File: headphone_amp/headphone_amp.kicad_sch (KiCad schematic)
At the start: 31 parts, among them J1 POWER, J2 INPUT, J3 PHONES, U1 LDL1117S50R, U2 LM4808

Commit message: Use kosmo-lib. Export PDF
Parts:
- removed U2: LM4808, Package_SO:SOIC-8_3.9x4.9mm_P1.27mm, symbol headphone_amp:LM4808
- added U2: LM4808, Package_SO:SOIC-8_3.9x4.9mm_P1.27mm, symbol kosmo-lib:LM4808
- RV1: footprint headphone_amp:Pot_Bourns_PTD902 -> kosmo-lib:Pot_Bourns_PTD902
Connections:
- net +5V: now also U2.8 (VDD)
- net AMP_BIAS: now also U2.3 (IN_A+), U2.5 (IN_B+)
- net AMP_IN_L: now also U2.2 (IN_A-)
- net AMP_IN_R: now also U2.6 (IN_B-)
- net AMP_OUT_L: now also U2.1 (OUT_A)
- net AMP_OUT_R: now also U2.7 (OUT_B)
- net GND: now also U2.4 (GND)
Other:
- company: (none) -> Max Proskauer
- title: (none) -> LM4808 Headphone Amp Module
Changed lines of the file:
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@@
 (kicad_sch (version 20211123) (generator eeschema)
   (paper "USLetter")
+  (title_block
+    (title "LM4808 Headphone Amp Module")
+    (date "2022-05-30")
+    (rev "0.1")
+    (company "Max Proskauer")
+  )
   (junction (at 91.44 158.75) (diameter 0) (color 0 0 0 0)
   )
@@
     (pin "1")
   )
-  (symbol (lib_id "Device:R") (at 86.36 83.82 0) (unit 1)
-    (in_bom yes) (on_board yes) (fields_autoplaced)
-    (property "Reference" "R2" (id 0) (at 88.9 82.5499 0)
-      (effects (font (size 1.27 1.27)) (justify left))
-    )
-    (property "Value" "100k" (id 1) (at 88.9 85.0899 0)
-      (effects (font (size 1.27 1.27)) (justify left))
-    )
-    (property "Footprint" "Resistor_THT:R_Axial_DIN0207_L6.3mm_D2.5mm_P10.16mm_Horizontal" (id 2) (at 84.582 83.82 90)
-      (effects (font (size 1.27 1.27)) hide)
-    )
-    (property "Datasheet" "~" (id 3) (at 86.36 83.82 0)
-      (effects (font (size 1.27 1.27)) hide)
-    )
-    (pin "1")
-    (pin "2")
-  )
-  (symbol (lib_id "Device:R_Potentiometer_Dual") (at 60.96 77.47 270) (mirror x) (unit 1)
-    (in_bom yes) (on_board yes)
-    (property "Reference" "RV1" (id 0) (at 54.61 69.85 90)
-      (effects (font (size 1.27 1.27)) (justify right))
-    )
-    (property "Value" "10k" (id 1) (at 54.61 72.39 90)
-      (effects (font (size 1.27 1.27)) (justify right))
-    )
-    (property "Footprint" "headphone_amp:Pot_Bourns_PTD902" (id 2) (at 59.055 71.12 0)
-      (effects (font (size 1.27 1.27)) hide)
-    )
-    (property "Datasheet" "~" (id 3) (at 59.055 71.12 0)
-      (effects (font (size 1.27 1.27)) hide)
-    )
-    (pin "1")
-    (pin "2")
-    (pin "3")
-    (pin "4")
-    (pin "5")
-    (pin "6")
-  )
-  (symbol (lib_id "Device:D") (at 201.93 115.57 270) (unit 1)
-    (in_bom yes) (on_board yes) (fields_autoplaced)
-    (property "Reference" "D5" (id 0) (at 204.47 114.2999 90)
-      (effects (font (size 1.27 1.27)) (justify left))
-    )
-    (property "Value" "1N4148" (id 1) (at 204.47 116.8399 90)
-      (effects (font (size 1.27 1.27)) (justify left))
-    )
-    (property "Footprint" "Diode_THT:D_DO-34_SOD68_P7.62mm_Horizontal" (id 2) (at 201.93 115.57 0)
-      (effects (font (size 1.27 1.27)) hide)
-    )
-    (property "Datasheet" "~" (id 3) (at 201.93 115.57 0)
-      (effects (font (size 1.27 1.27)) hide)
-    )
-    (pin "1")
-    (pin "2")
-  )
-  (symbol (lib_id "power:-12V") (at 201.93 58.42 180) (unit 1)
-    (in_bom yes) (on_board yes)
-    (property "Reference" "#PWR021" (id 0) (at 201.93 60.96 0)
-      (effects (font (size 1.27 1.27)) hide)
-    )
-    (property "Value" "-12V" (id 1) (at 201.93 62.23 0))
-    (property "Footprint" "" (id 2) (at 201.93 58.42 0)
-      (effects (font (size 1.27 1.27)) hide)
-    )
-    (property "Datasheet" "" (id 3) (at 201.93 58.42 0)
-      (effects (font (size 1.27 1.27)) hide)
-    )
-    (pin "1")
-  )
-  (symbol (lib_id "headphone_amp:LM4808") (at 140.97 77.47 0) (unit 1)
+  (symbol (lib_id "kosmo-lib:LM4808") (at 140.97 77.47 0) (unit 1)
     (in_bom yes) (on_board yes)
     (property "Reference" "U2" (id 0) (at 132.08 57.15 0)
@@
     (pin "7")
     (pin "8")
+  )
+  (symbol (lib_id "Device:R") (at 86.36 83.82 0) (unit 1)
+    (in_bom yes) (on_board yes) (fields_autoplaced)
+    (property "Reference" "R2" (id 0) (at 88.9 82.5499 0)
+      (effects (font (size 1.27 1.27)) (justify left))
+    )
+    (property "Value" "100k" (id 1) (at 88.9 85.0899 0)
+      (effects (font (size 1.27 1.27)) (justify left))
+    )
+    (property "Footprint" "Resistor_THT:R_Axial_DIN0207_L6.3mm_D2.5mm_P10.16mm_Horizontal" (id 2) (at 84.582 83.82 90)
+      (effects (font (size 1.27 1.27)) hide)
+    )
+    (property "Datasheet" "~" (id 3) (at 86.36 83.82 0)
+      (effects (font (size 1.27 1.27)) hide)
+    )
+    (pin "1")
+    (pin "2")
+  )
+  (symbol (lib_id "Device:R_Potentiometer_Dual") (at 60.96 77.47 270) (mirror x) (unit 1)
+    (in_bom yes) (on_board yes)
+    (property "Reference" "RV1" (id 0) (at 54.61 69.85 90)
+      (effects (font (size 1.27 1.27)) (justify right))
+    )
+    (property "Value" "10k" (id 1) (at 54.61 72.39 90)
+      (effects (font (size 1.27 1.27)) (justify right))
+    )
+    (property "Footprint" "kosmo-lib:Pot_Bourns_PTD902" (id 2) (at 59.055 71.12 0)
+      (effects (font (size 1.27 1.27)) hide)
+    )
+    (property "Datasheet" "~" (id 3) (at 59.055 71.12 0)
+      (effects (font (size 1.27 1.27)) hide)
+    )
+    (pin "1")
+    (pin "2")
+    (pin "3")
+    (pin "4")
+    (pin "5")
+    (pin "6")
+  )
+  (symbol (lib_id "Device:D") (at 201.93 115.57 270) (unit 1)
+    (in_bom yes) (on_board yes) (fields_autoplaced)
+    (property "Reference" "D5" (id 0) (at 204.47 114.2999 90)
+      (effects (font (size 1.27 1.27)) (justify left))
+    )
+    (property "Value" "1N4148" (id 1) (at 204.47 116.8399 90)
+      (effects (font (size 1.27 1.27)) (justify left))
+    )
+    (property "Footprint" "Diode_THT:D_DO-34_SOD68_P7.62mm_Horizontal" (id 2) (at 201.93 115.57 0)
+      (effects (font (size 1.27 1.27)) hide)
+    )
+    (property "Datasheet" "~" (id 3) (at 201.93 115.57 0)
+      (effects (font (size 1.27 1.27)) hide)
+    )
+    (pin "1")
+    (pin "2")
+  )
+  (symbol (lib_id "power:-12V") (at 201.93 58.42 180) (unit 1)
+    (in_bom yes) (on_board yes)
+    (property "Reference" "#PWR021" (id 0) (at 201.93 60.96 0)
+      (effects (font (size 1.27 1.27)) hide)
+    )
+    (property "Value" "-12V" (id 1) (at 201.93 62.23 0))
+    (property "Footprint" "" (id 2) (at 201.93 58.42 0)
+      (effects (font (size 1.27 1.27)) hide)
+    )
+    (property "Datasheet" "" (id 3) (at 201.93 58.42 0)
+      (effects (font (size 1.27 1.27)) hide)
+    )
+    (pin "1")
   )
   (symbol (lib_id "power:+12V") (at 91.44 156.21 0) (unit 1)
@@
     )
     (path "/1eaa0cb5-51d1-4401-b7ff-689d85613c1f"
-      (reference "RV1") (unit 1) (value "10k") (footprint "headphone_amp:Pot_Bourns_PTD902")
+      (reference "RV1") (unit 1) (value "10k") (footprint "kosmo-lib:Pot_Bourns_PTD902")
     )
     (path "/05cac65d-cafa-4294-bc5f-223d82790f31"
       (reference "U1") (unit 1) (value "LDL1117S50R") (footprint "Package_TO_SOT_SMD:SOT-223-3_TabPin2")
     )
-    (path "/320fed46-77b3-4eb5-bc13-110c5a80010f"
+    (path "/0e73a828-0418-4f17-8d62-78e994dcde5c"
       (reference "U2") (unit 1) (value "LM4808") (footprint "Package_SO:SOIC-8_3.9x4.9mm_P1.27mm")
     )

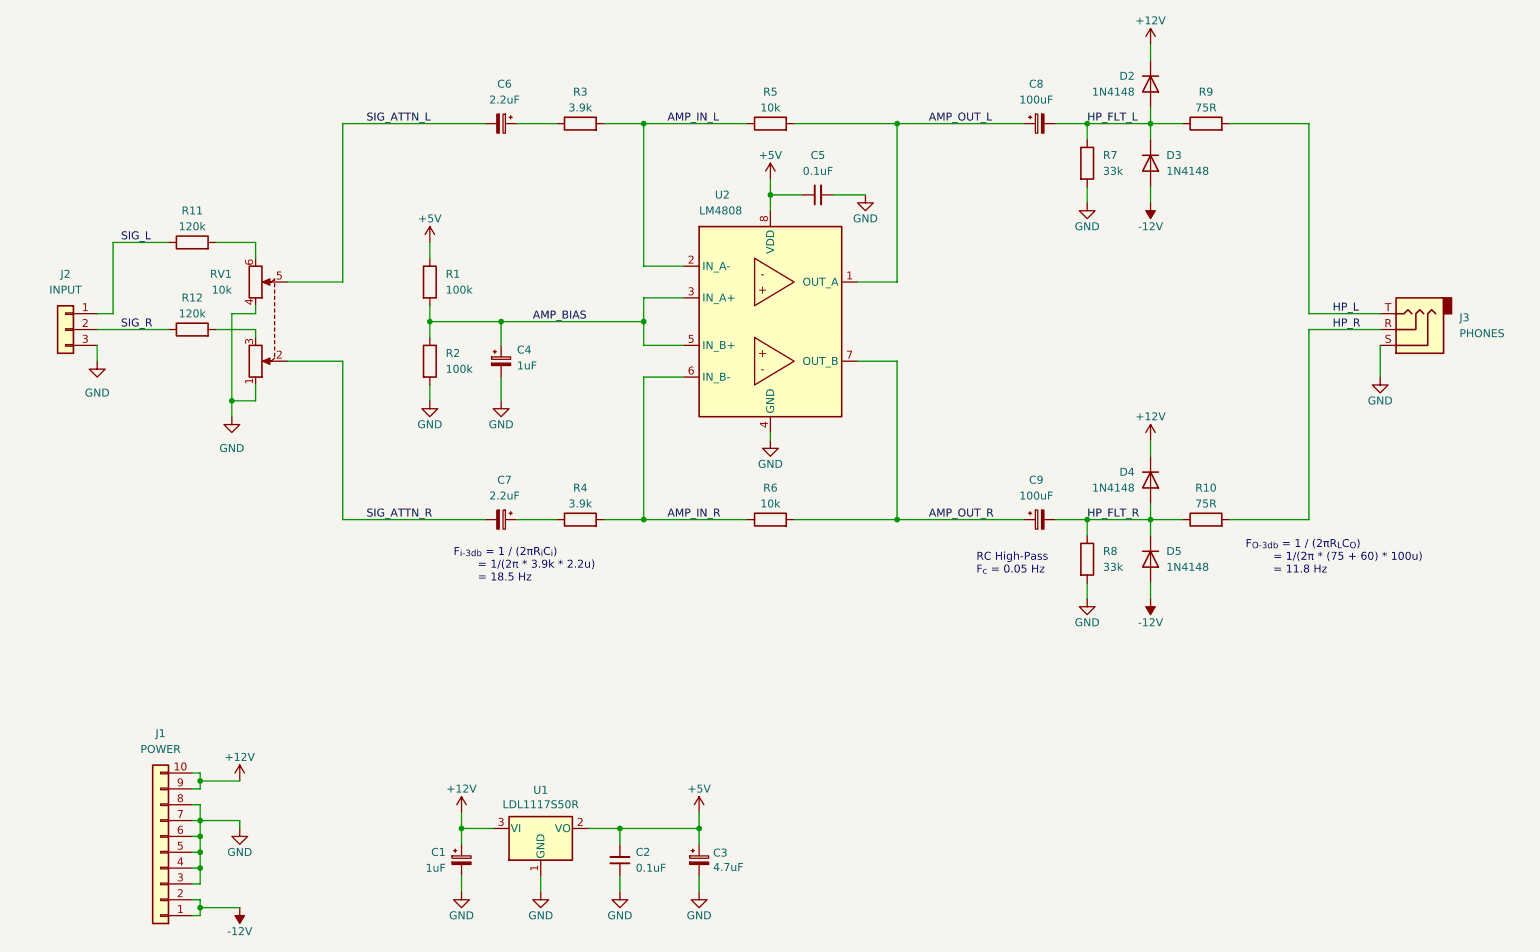
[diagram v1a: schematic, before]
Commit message: Add mono jumper
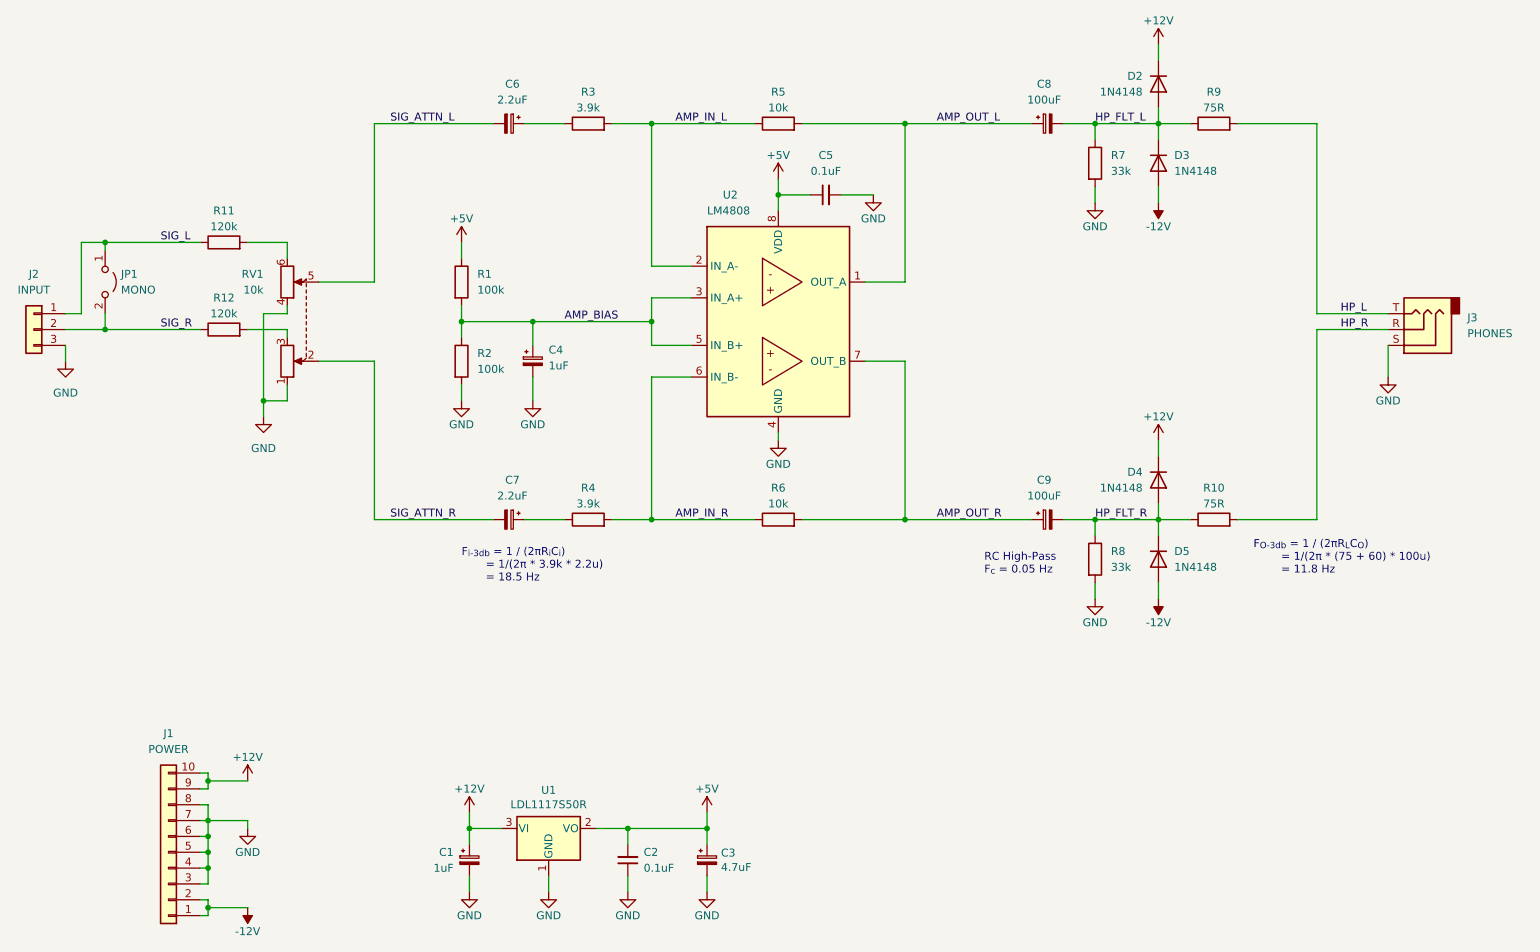
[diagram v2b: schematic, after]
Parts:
- added JP1: MONO, Connector_PinHeader_2.54mm:PinHeader_1x02_P2.54mm_Vertical, symbol Jumper:Jumper_2_Open
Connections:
- net SIG_L: now also JP1.1 (A)
- net SIG_R: now also JP1.2 (B)
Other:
- moved on the sheet: C1, C2, C3, C4, C5, C6, C7, C8, C9, D2, D3, D4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
